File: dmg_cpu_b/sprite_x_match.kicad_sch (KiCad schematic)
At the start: 115 parts

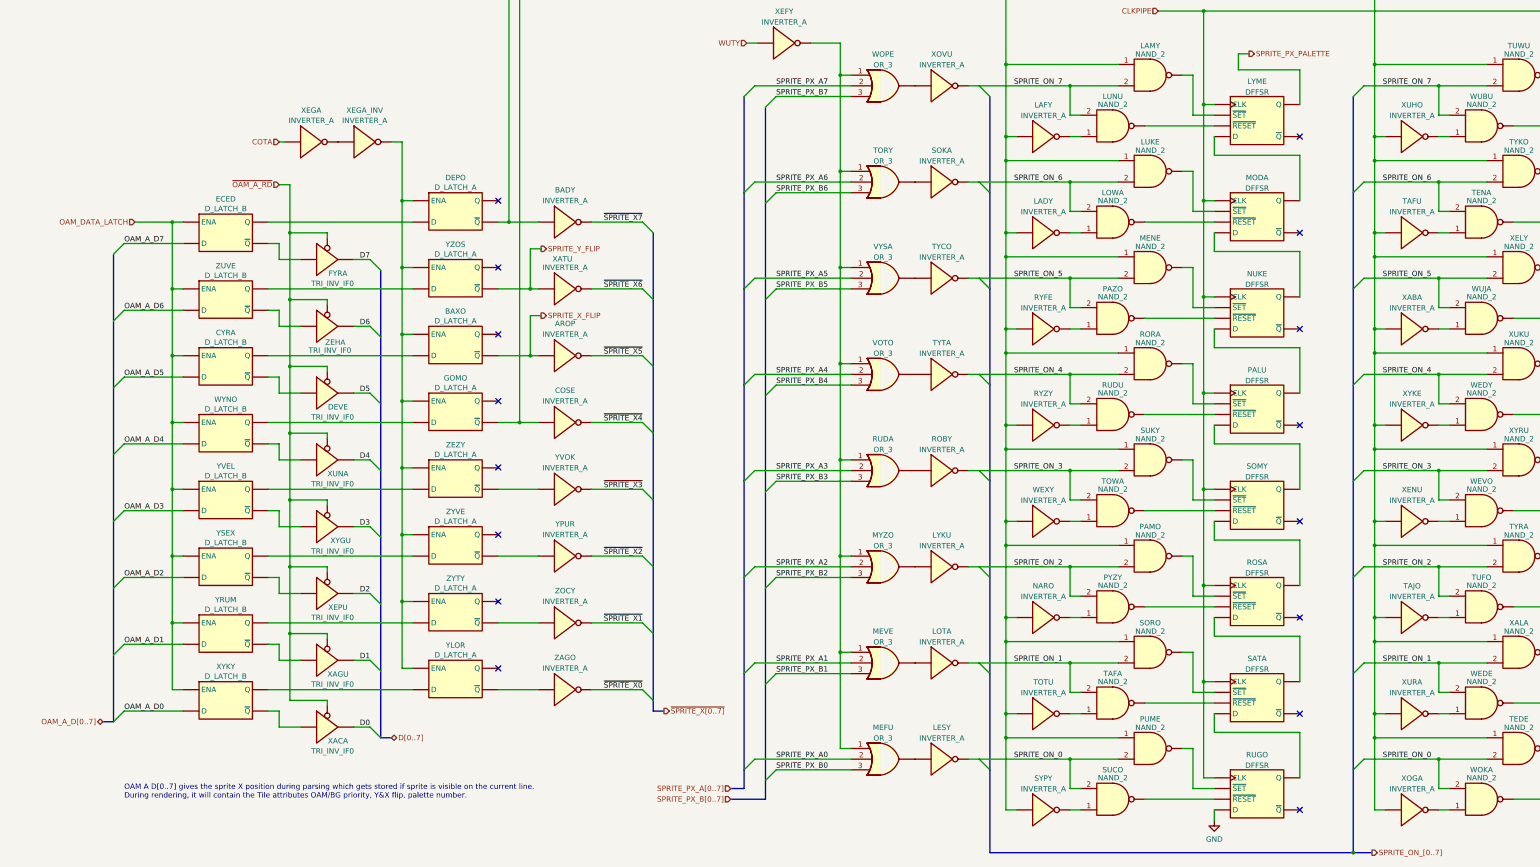
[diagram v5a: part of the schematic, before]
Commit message: Issues addressed. Renaming and inverted signal names to make thing more consistent and meaningful.
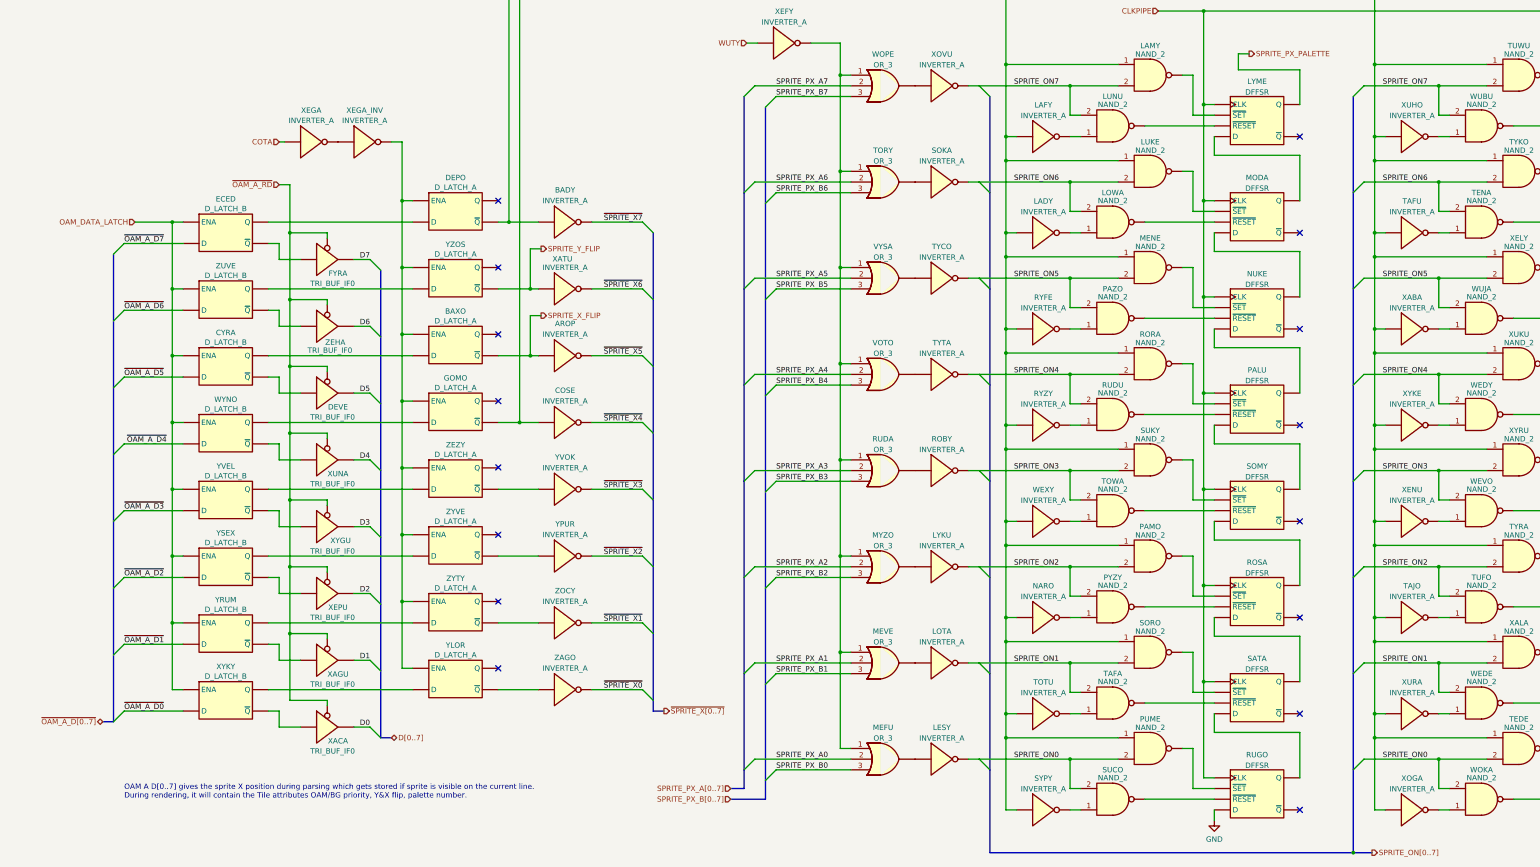
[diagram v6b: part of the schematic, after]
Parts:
- DEVE, FYRA, XACA, XAGU, XEPU, XUNA, XYGU, ZEHA: value TRI_INV_IF0 -> TRI_BUF_IF0
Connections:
- net OAM_A_D0 renamed ~{OAM_A_D0}
- net OAM_A_D1 renamed ~{OAM_A_D1}
- net OAM_A_D2 renamed ~{OAM_A_D2}
- net OAM_A_D3 renamed ~{OAM_A_D3}
- net OAM_A_D4 renamed ~{OAM_A_D4}
- net OAM_A_D5 renamed ~{OAM_A_D5}
- net OAM_A_D6 renamed ~{OAM_A_D6}
- net OAM_A_D7 renamed ~{OAM_A_D7}
- net SPRITE_ON_0 renamed SPRITE_ON0
- net SPRITE_ON_1 renamed SPRITE_ON1
- net SPRITE_ON_2 renamed SPRITE_ON2
- net SPRITE_ON_3 renamed SPRITE_ON3
- net SPRITE_ON_4 renamed SPRITE_ON4
- net SPRITE_ON_5 renamed SPRITE_ON5
- net SPRITE_ON_6 renamed SPRITE_ON6
- net SPRITE_ON_7 renamed SPRITE_ON7
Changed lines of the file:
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@@
     (effects (font (size 1.27 1.27)) (justify left bottom))
   )
-  (label "SPRITE_ON_5" (at 245.745 99.695 0)
-    (effects (font (size 1.27 1.27)) (justify left bottom))
-  )
-  (label "SPRITE_ON_3" (at 333.375 145.415 0)
+  (label "SPRITE_ON5" (at 245.745 99.695 0)
+    (effects (font (size 1.27 1.27)) (justify left bottom))
+  )
+  (label "SPRITE_ON3" (at 333.375 145.415 0)
     (effects (font (size 1.27 1.27)) (justify left bottom))
   )
@@
     (effects (font (size 1.27 1.27)) (justify left bottom))
   )
-  (label "SPRITE_ON_4" (at 333.375 122.555 0)
+  (label "SPRITE_ON4" (at 333.375 122.555 0)
     (effects (font (size 1.27 1.27)) (justify left bottom))
   )
@@
     (effects (font (size 1.27 1.27)) (justify left bottom))
   )
-  (label "SPRITE_ON_2" (at 245.745 168.275 0)
+  (label "SPRITE_ON2" (at 245.745 168.275 0)
     (effects (font (size 1.27 1.27)) (justify left bottom))
   )
@@
     (effects (font (size 1.27 1.27)) (justify right bottom))
   )
-  (label "OAM_A_D7" (at 34.29 91.44 0)
-    (effects (font (size 1.27 1.27)) (justify left bottom))
-  )
-  (label "SPRITE_ON_6" (at 245.745 76.835 0)
-    (effects (font (size 1.27 1.27)) (justify left bottom))
-  )
-  (label "SPRITE_ON_1" (at 333.375 191.135 0)
-    (effects (font (size 1.27 1.27)) (justify left bottom))
-  )
-  (label "SPRITE_ON_5" (at 333.375 99.695 0)
+  (label "SPRITE_ON6" (at 245.745 76.835 0)
+    (effects (font (size 1.27 1.27)) (justify left bottom))
+  )
+  (label "SPRITE_ON1" (at 333.375 191.135 0)
+    (effects (font (size 1.27 1.27)) (justify left bottom))
+  )
+  (label "~{OAM_A_D4}" (at 34.925 139.065 0)
+    (effects (font (size 1.27 1.27)) (justify left bottom))
+  )
+  (label "~{OAM_A_D6}" (at 34.29 107.315 0)
+    (effects (font (size 1.27 1.27)) (justify left bottom))
+  )
+  (label "~{OAM_A_D3}" (at 34.29 154.94 0)
+    (effects (font (size 1.27 1.27)) (justify left bottom))
+  )
+  (label "SPRITE_ON5" (at 333.375 99.695 0)
     (effects (font (size 1.27 1.27)) (justify left bottom))
   )
@@
     (effects (font (size 1.27 1.27)) (justify left bottom))
   )
-  (label "SPRITE_ON_0" (at 245.745 213.995 0)
+  (label "SPRITE_ON0" (at 245.745 213.995 0)
     (effects (font (size 1.27 1.27)) (justify left bottom))
   )
@@
     (effects (font (size 1.27 1.27)) (justify left bottom))
   )
-  (label "SPRITE_ON_7" (at 245.745 53.975 0)
+  (label "~{OAM_A_D1}" (at 34.29 186.69 0)
+    (effects (font (size 1.27 1.27)) (justify left bottom))
+  )
+  (label "SPRITE_ON7" (at 245.745 53.975 0)
     (effects (font (size 1.27 1.27)) (justify left bottom))
   )
@@
     (effects (font (size 1.27 1.27)) (justify left bottom))
   )
-  (label "OAM_A_D2" (at 34.29 170.815 0)
-    (effects (font (size 1.27 1.27)) (justify left bottom))
-  )
-  (label "SPRITE_ON_0" (at 333.375 213.995 0)
-    (effects (font (size 1.27 1.27)) (justify left bottom))
-  )
-  (label "SPRITE_ON_2" (at 333.375 168.275 0)
+  (label "SPRITE_ON0" (at 333.375 213.995 0)
+    (effects (font (size 1.27 1.27)) (justify left bottom))
+  )
+  (label "SPRITE_ON2" (at 333.375 168.275 0)
+    (effects (font (size 1.27 1.27)) (justify left bottom))
+  )
+  (label "~{OAM_A_D0}" (at 34.29 202.565 0)
     (effects (font (size 1.27 1.27)) (justify left bottom))
   )
@@
     (effects (font (size 1.27 1.27)) (justify left bottom))
   )
-  (label "SPRITE_ON_7" (at 333.375 53.975 0)
-    (effects (font (size 1.27 1.27)) (justify left bottom))
-  )
-  (label "OAM_A_D3" (at 34.29 154.94 0)
+  (label "SPRITE_ON7" (at 333.375 53.975 0)
     (effects (font (size 1.27 1.27)) (justify left bottom))
   )
@@
     (effects (font (size 1.27 1.27)) (justify right bottom))
   )
-  (label "OAM_A_D0" (at 34.29 202.565 0)
-    (effects (font (size 1.27 1.27)) (justify left bottom))
-  )
-  (label "OAM_A_D6" (at 34.29 107.315 0)
-    (effects (font (size 1.27 1.27)) (justify left bottom))
-  )
   (label "SPRITE_PX_B2" (at 189.23 170.815 0)
     (effects (font (size 1.27 1.27)) (justify left bottom))
@@
     (effects (font (size 1.27 1.27)) (justify right bottom))
   )
+  (label "~{OAM_A_D2}" (at 34.29 170.815 0)
+    (effects (font (size 1.27 1.27)) (justify left bottom))
+  )
   (label "D3" (at 92.71 158.75 180)
     (effects (font (size 1.27 1.27)) (justify right bottom))
@@
     (effects (font (size 1.27 1.27)) (justify right bottom))
   )
-  (label "SPRITE_ON_6" (at 333.375 76.835 0)
+  (label "SPRITE_ON6" (at 333.375 76.835 0)
     (effects (font (size 1.27 1.27)) (justify left bottom))
   )
@@
     (effects (font (size 1.27 1.27)) (justify right bottom))
   )
+  (label "~{OAM_A_D5}" (at 34.29 123.19 0)
+    (effects (font (size 1.27 1.27)) (justify left bottom))
+  )
   (label "~{SPRITE_X6}" (at 157.48 102.235 180)
     (effects (font (size 1.27 1.27)) (justify right bottom))
@@
     (effects (font (size 1.27 1.27)) (justify right bottom))
   )
-  (label "SPRITE_ON_1" (at 245.745 191.135 0)
+  (label "SPRITE_ON1" (at 245.745 191.135 0)
     (effects (font (size 1.27 1.27)) (justify left bottom))
   )
   (label "SPRITE_PX_B1" (at 189.23 193.675 0)
+    (effects (font (size 1.27 1.27)) (justify left bottom))
+  )
+  (label "~{OAM_A_D7}" (at 34.29 91.44 0)
     (effects (font (size 1.27 1.27)) (justify left bottom))
   )
@@
     (effects (font (size 1.27 1.27)) (justify right bottom))
   )
-  (label "OAM_A_D5" (at 34.29 123.19 0)
-    (effects (font (size 1.27 1.27)) (justify left bottom))
-  )
-  (label "SPRITE_ON_4" (at 245.745 122.555 0)
-    (effects (font (size 1.27 1.27)) (justify left bottom))
-  )
-  (label "OAM_A_D4" (at 34.29 139.065 0)
+  (label "SPRITE_ON4" (at 245.745 122.555 0)
     (effects (font (size 1.27 1.27)) (justify left bottom))
   )
@@
     (effects (font (size 1.27 1.27)) (justify left bottom))
   )
-  (label "SPRITE_ON_3" (at 245.745 145.415 0)
-    (effects (font (size 1.27 1.27)) (justify left bottom))
-  )
-  (label "OAM_A_D1" (at 34.29 186.69 0)
+  (label "SPRITE_ON3" (at 245.745 145.415 0)
     (effects (font (size 1.27 1.27)) (justify left bottom))
   )
@@
     (effects (font (size 1.27 1.27)) (justify left))
   )
-  (hierarchical_label "OAM_A_D[0..7]" (shape bidirectional) (at 29.21 205.105 180)
+  (hierarchical_label "~{OAM_A_D[0..7]}" (shape bidirectional) (at 29.21 205.105 180)
     (effects (font (size 1.27 1.27)) (justify right))
   )
@@
     (effects (font (size 1.27 1.27)) (justify left))
   )
-  (hierarchical_label "SPRITE_ON_[0..7]" (shape output) (at 330.835 236.22 0)
+  (hierarchical_label "SPRITE_ON[0..7]" (shape output) (at 330.835 236.22 0)
     (effects (font (size 1.27 1.27)) (justify left))
   )
@@
     (in_bom yes) (on_board yes)
     (property "Reference" "XAGU" (id 0) (at 85.09 193.802 0))
-    (property "Value" "TRI_INV_IF0" (id 1) (at 83.82 196.215 0))
+    (property "Value" "TRI_BUF_IF0" (id 1) (at 83.82 196.215 0))
     (property "Footprint" "" (id 2) (at 80.01 190.5 0)
       (effects (font (size 1.27 1.27)) hide)
@@
   (symbol (lib_id "power:GND") (at 293.37 228.6 0) (unit 1)
     (in_bom yes) (on_board yes) (fields_autoplaced)
-    (property "Reference" "#PWR?" (id 0) (at 293.37 234.95 0)
+    (property "Reference" "#PWR0128" (id 0) (at 293.37 234.95 0)
       (effects (font (size 1.27 1.27)) hide)
     )
@@
     (in_bom yes) (on_board yes)
     (property "Reference" "DEVE" (id 0) (at 85.09 130.302 0))
-    (property "Value" "TRI_INV_IF0" (id 1) (at 83.82 132.715 0))
+    (property "Value" "TRI_BUF_IF0" (id 1) (at 83.82 132.715 0))
     (property "Footprint" "" (id 2) (at 80.01 127 0)
       (effects (font (size 1.27 1.27)) hide)
@@
     (in_bom yes) (on_board yes)
     (property "Reference" "XEPU" (id 0) (at 85.09 177.927 0))
-    (property "Value" "TRI_INV_IF0" (id 1) (at 83.82 180.34 0))
+    (property "Value" "TRI_BUF_IF0" (id 1) (at 83.82 180.34 0))
     (property "Footprint" "" (id 2) (at 80.01 174.625 0)
       (effects (font (size 1.27 1.27)) hide)
@@
     (in_bom yes) (on_board yes)
     (property "Reference" "XACA" (id 0) (at 85.09 209.677 0))
-    (property "Value" "TRI_INV_IF0" (id 1) (at 83.82 212.09 0))
+    (property "Value" "TRI_BUF_IF0" (id 1) (at 83.82 212.09 0))
     (property "Footprint" "" (id 2) (at 80.01 206.375 0)
       (effects (font (size 1.27 1.27)) hide)
@@
     (in_bom yes) (on_board yes)
     (property "Reference" "ZEHA" (id 0) (at 84.455 114.935 0))
-    (property "Value" "TRI_INV_IF0" (id 1) (at 83.185 116.84 0))
+    (property "Value" "TRI_BUF_IF0" (id 1) (at 83.185 116.84 0))
     (property "Footprint" "" (id 2) (at 80.01 111.125 0)
       (effects (font (size 1.27 1.27)) hide)
@@
     (in_bom yes) (on_board yes)
     (property "Reference" "XYGU" (id 0) (at 85.725 162.052 0))
-    (property "Value" "TRI_INV_IF0" (id 1) (at 83.82 164.592 0))
+    (property "Value" "TRI_BUF_IF0" (id 1) (at 83.82 164.592 0))
     (property "Footprint" "" (id 2) (at 80.01 158.75 0)
       (effects (font (size 1.27 1.27)) hide)
@@
     (in_bom yes) (on_board yes)
     (property "Reference" "FYRA" (id 0) (at 85.09 98.552 0))
-    (property "Value" "TRI_INV_IF0" (id 1) (at 83.82 100.965 0))
+    (property "Value" "TRI_BUF_IF0" (id 1) (at 83.82 100.965 0))
     (property "Footprint" "" (id 2) (at 80.01 95.25 0)
       (effects (font (size 1.27 1.27)) hide)
@@
   (symbol (lib_id "power:+5V") (at 374.015 230.505 0) (unit 1)
     (in_bom yes) (on_board yes) (fields_autoplaced)
-    (property "Reference" "#PWR?" (id 0) (at 374.015 234.315 0)
+    (property "Reference" "#PWR0127" (id 0) (at 374.015 234.315 0)
       (effects (font (size 1.27 1.27)) hide)
     )
@@
     (in_bom yes) (on_board yes)
     (property "Reference" "XUNA" (id 0) (at 85.09 146.177 0))
-    (property "Value" "TRI_INV_IF0" (id 1) (at 83.82 148.59 0))
+    (property "Value" "TRI_BUF_IF0" (id 1) (at 83.82 148.59 0))
     (property "Footprint" "" (id 2) (at 80.01 142.875 0)
       (effects (font (size 1.27 1.27)) hide)

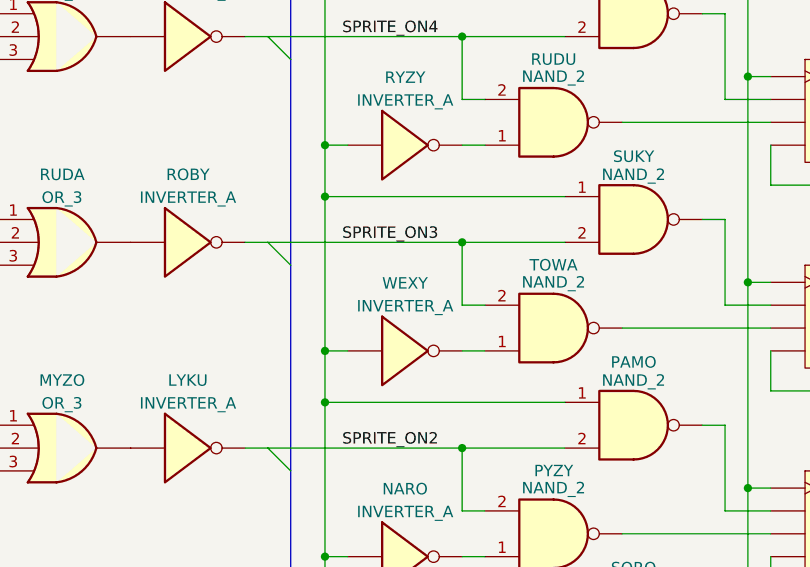
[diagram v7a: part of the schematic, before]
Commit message: Rename cells: BABA, BOFO, TOMA and WEXY
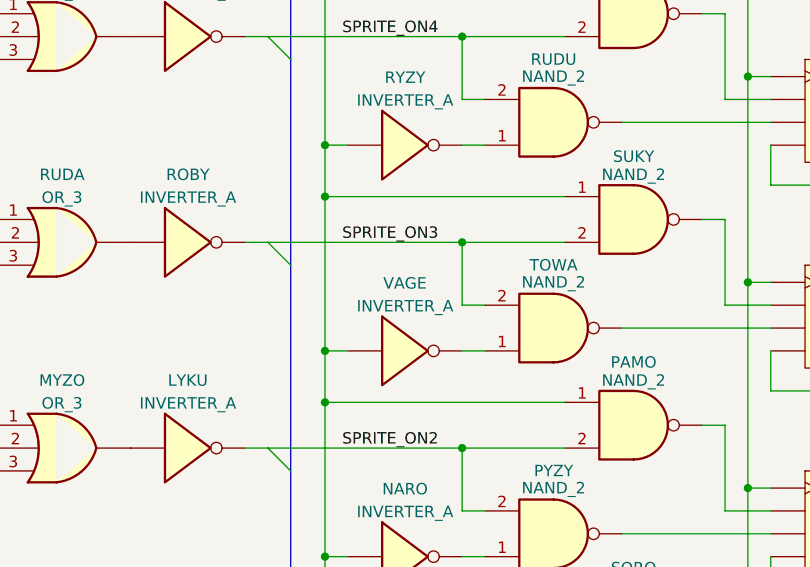
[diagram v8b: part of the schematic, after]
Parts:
- renumbered WEXY to VAGE
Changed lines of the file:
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@@
   (symbol (lib_id "DMG_CPU_Cells:INVERTER_A") (at 252.73 157.48 0) (unit 1)
     (in_bom yes) (on_board yes) (fields_autoplaced)
-    (property "Reference" "WEXY" (id 0) (at 252.73 149.9702 0))
+    (property "Reference" "VAGE" (id 0) (at 252.73 149.9702 0))
     (property "Value" "INVERTER_A" (id 1) (at 252.73 152.5071 0))
     (property "Footprint" "" (id 2) (at 250.19 157.48 0)
